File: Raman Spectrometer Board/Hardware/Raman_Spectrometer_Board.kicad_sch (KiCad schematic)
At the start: 16 parts, among them J1 RJ45_LED_Shielded, J2 Conn_01x05_Pin, J3 Conn_01x03_Pin, Q1 BSS138, U1 Teensy4.1_DEV-16771, U2 OKI

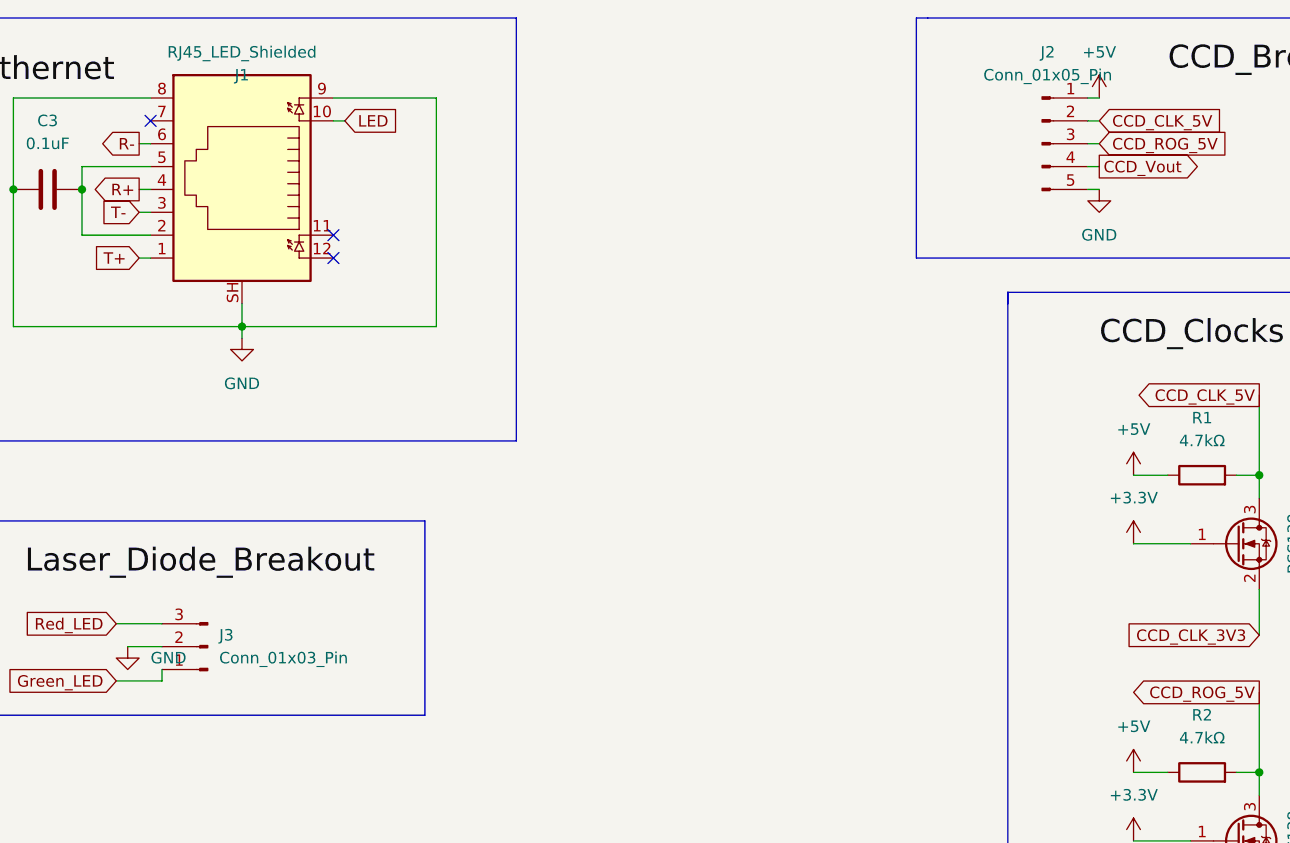
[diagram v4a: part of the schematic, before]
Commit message: fix: switched connectors to Molex
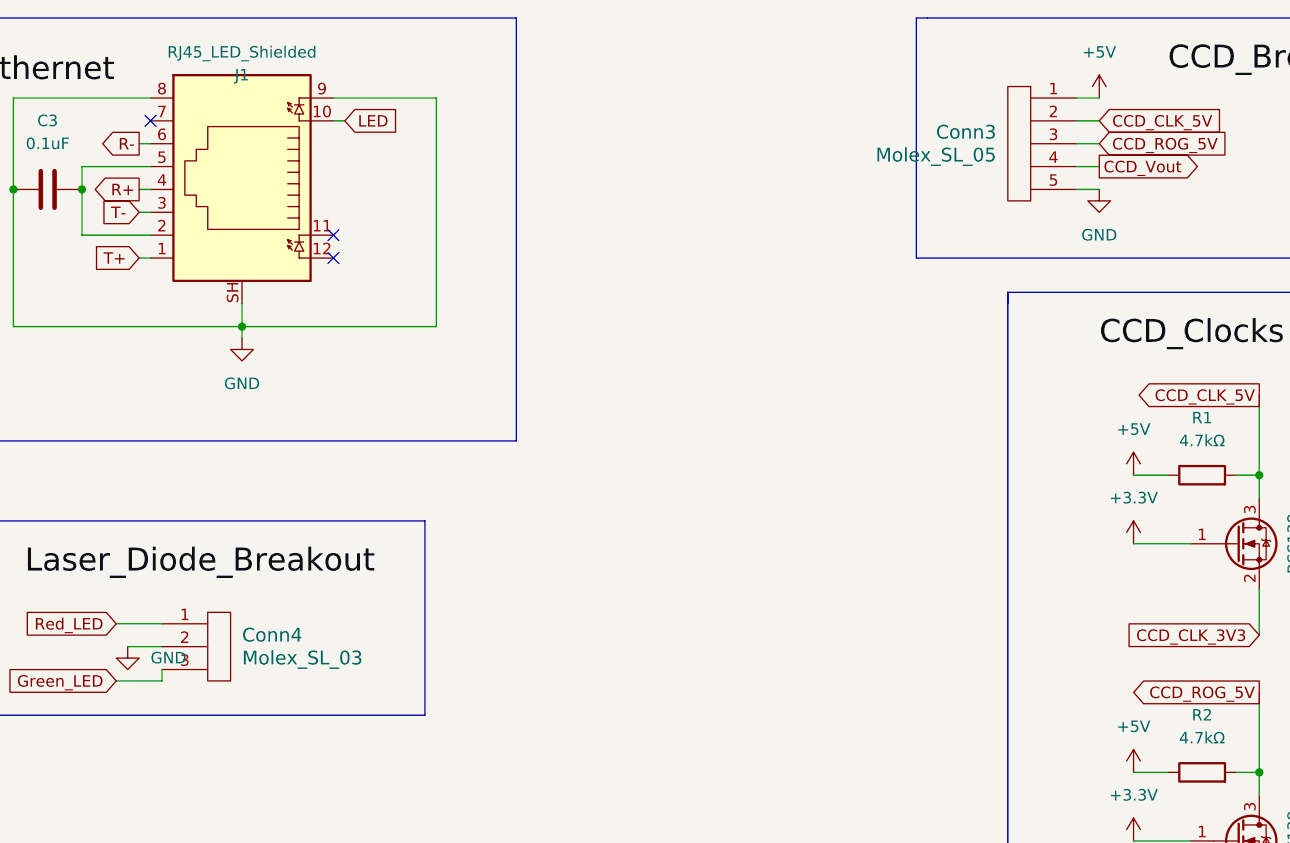
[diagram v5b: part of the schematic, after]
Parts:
- removed J2: Conn_01x05_Pin, symbol Connector:Conn_01x05_Pin
- removed J3: Conn_01x03_Pin, symbol Connector:Conn_01x03_Pin
- added Conn3: Molex_SL_05, symbol MRDT_Connectors:Molex_SL_05
- added Conn4: Molex_SL_03, symbol MRDT_Connectors:Molex_SL_03
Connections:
- net +5V: now also Conn3.1
- net CCD_CLK_5V: now also Conn3.2
- net CCD_ROG_5V: now also Conn3.3
- net CCD_Vout: now also Conn3.4
- net GND: now also Conn3.5, Conn4.2
- net Green_LED: now also Conn4.3
- net Red_LED: now also Conn4.1
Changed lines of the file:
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@@
-    (stroke (width 0) (type default))
-  )
-  (wire (pts (xy 243.84 22.86) (xy 245.11 22.86))
     (stroke (width 0) (type default))
   )
@@
     (stroke (width 0) (type default))
   )
+  (wire (pts (xy 242.57 22.86) (xy 245.11 22.86))
+    (stroke (width 0) (type default))
+  )
   (wire (pts (xy 82.55 135.89) (xy 81.28 135.89))
     (stroke (width 0) (type default))
@@
     (stroke (width 0) (type default))
   )
-  (wire (pts (xy 243.84 33.02) (xy 245.11 33.02))
+  (wire (pts (xy 242.57 33.02) (xy 245.11 33.02))
     (stroke (width 0) (type default))
   )
@@
     (stroke (width 0) (type default))
   )
-  (wire (pts (xy 243.84 27.94) (xy 245.11 27.94))
+  (wire (pts (xy 242.57 27.94) (xy 245.11 27.94))
     (stroke (width 0) (type default))
   )
@@
     (stroke (width 0) (type default))
   )
-  (wire (pts (xy 243.84 25.4) (xy 245.11 25.4))
-    (stroke (width 0) (type default))
-  )
   (polyline (pts (xy 115.57 13.97) (xy 115.57 60.96))
     (stroke (width 0) (type default))
@@
     (stroke (width 0) (type default))
   )
-  (wire (pts (xy 243.84 30.48) (xy 245.11 30.48))
+  (wire (pts (xy 242.57 30.48) (xy 245.11 30.48))
     (stroke (width 0) (type default))
   )
@@
   )
   (polyline (pts (xy 234.95 121.92) (xy 242.57 121.92))
+    (stroke (width 0) (type default))
+  )
+  (wire (pts (xy 242.57 25.4) (xy 245.11 25.4))
     (stroke (width 0) (type default))
   )
@@
     )
   )
+  (symbol (lib_id "MRDT_Connectors:Molex_SL_03") (at 146.05 87.63 0) (unit 1)
+    (in_bom yes) (on_board yes) (dnp no) (fields_autoplaced)
+    (property "Reference" "Conn4" (at 149.86 82.55 0)
+      (effects (font (size 1.524 1.524)) (justify left))
+    )
+    (property "Value" "Molex_SL_03" (at 149.86 85.09 0)
+      (effects (font (size 1.524 1.524)) (justify left))
+    )
+    (property "Footprint" "" (at 146.05 87.63 0)
+      (effects (font (size 1.524 1.524)) hide)
+    )
+    (property "Datasheet" "" (at 146.05 87.63 0)
+      (effects (font (size 1.524 1.524)) hide)
+    )
+    (pin "1")
+    (pin "2")
+    (pin "3")
+    (instances
+      (project "Raman_Spectrometer_Board"
+        (path "/dd57774e-6364-4f58-a24d-9970470de2f9"
+          (reference "Conn4") (unit 1)
+        )
+      )
+    )
+  )
   (symbol (lib_id "Device:C") (at 128.27 33.02 270) (unit 1)
     (in_bom yes) (on_board yes) (dnp no) (fields_autoplaced)
@@
         (path "/dd57774e-6364-4f58-a24d-9970470de2f9"
           (reference "#PWR01") (unit 1)
-        )
-      )
-    )
-  )
-  (symbol (lib_id "Connector:Conn_01x05_Pin") (at 238.76 27.94 0) (unit 1)
-    (in_bom yes) (on_board yes) (dnp no) (fields_autoplaced)
-    (property "Reference" "J2" (at 239.395 17.78 0)
-      (effects (font (size 1.27 1.27)))
-    )
-    (property "Value" "Conn_01x05_Pin" (at 239.395 20.32 0)
-      (effects (font (size 1.27 1.27)))
-    )
-    (property "Footprint" "" (at 238.76 27.94 0)
-      (effects (font (size 1.27 1.27)) hide)
-    )
-    (property "Datasheet" "~" (at 238.76 27.94 0)
-      (effects (font (size 1.27 1.27)) hide)
-    )
-    (pin "1")
-    (pin "2")
-    (pin "3")
-    (pin "4")
-    (pin "5")
-    (instances
-      (project "Raman_Spectrometer_Board"
-        (path "/dd57774e-6364-4f58-a24d-9970470de2f9"
-          (reference "J2") (unit 1)
-        )
-      )
-    )
-  )
-  (symbol (lib_id "Connector:Conn_01x03_Pin") (at 146.05 83.82 180) (unit 1)
-    (in_bom yes) (on_board yes) (dnp no) (fields_autoplaced)
-    (property "Reference" "J3" (at 147.32 82.55 0)
-      (effects (font (size 1.27 1.27)) (justify right))
-    )
-    (property "Value" "Conn_01x03_Pin" (at 147.32 85.09 0)
-      (effects (font (size 1.27 1.27)) (justify right))
-    )
-    (property "Footprint" "" (at 146.05 83.82 0)
-      (effects (font (size 1.27 1.27)) hide)
-    )
-    (property "Datasheet" "~" (at 146.05 83.82 0)
-      (effects (font (size 1.27 1.27)) hide)
-    )
-    (pin "1")
-    (pin "2")
-    (pin "3")
-    (instances
-      (project "Raman_Spectrometer_Board"
-        (path "/dd57774e-6364-4f58-a24d-9970470de2f9"
-          (reference "J3") (unit 1)
         )
       )
@@
         )
       )
+    )
+  )
+  (symbol (lib_id "MRDT_Connectors:Molex_SL_05") (at 237.49 34.29 0) (mirror y) (unit 1)
+    (in_bom yes) (on_board yes) (dnp no)
+    (property "Reference" "Conn3" (at 233.68 26.67 0)
+      (effects (font (size 1.524 1.524)) (justify left))
+    )
+    (property "Value" "Molex_SL_05" (at 233.68 29.21 0)
+      (effects (font (size 1.524 1.524)) (justify left))
+    )
+    (property "Footprint" "" (at 237.49 34.29 0)
+      (effects (font (size 1.524 1.524)) hide)
+    )
+    (property "Datasheet" "" (at 237.49 34.29 0)
+      (effects (font (size 1.524 1.524)) hide)
+    )
+    (pin "1")
+    (pin "2")
+    (pin "3")
+    (pin "4")
+    (pin "5")
+    (instances
+      (project "Raman_Spectrometer_Board"
+        (path "/dd57774e-6364-4f58-a24d-9970470de2f9"
+          (reference "Conn3") (unit 1)
+        )
+      )

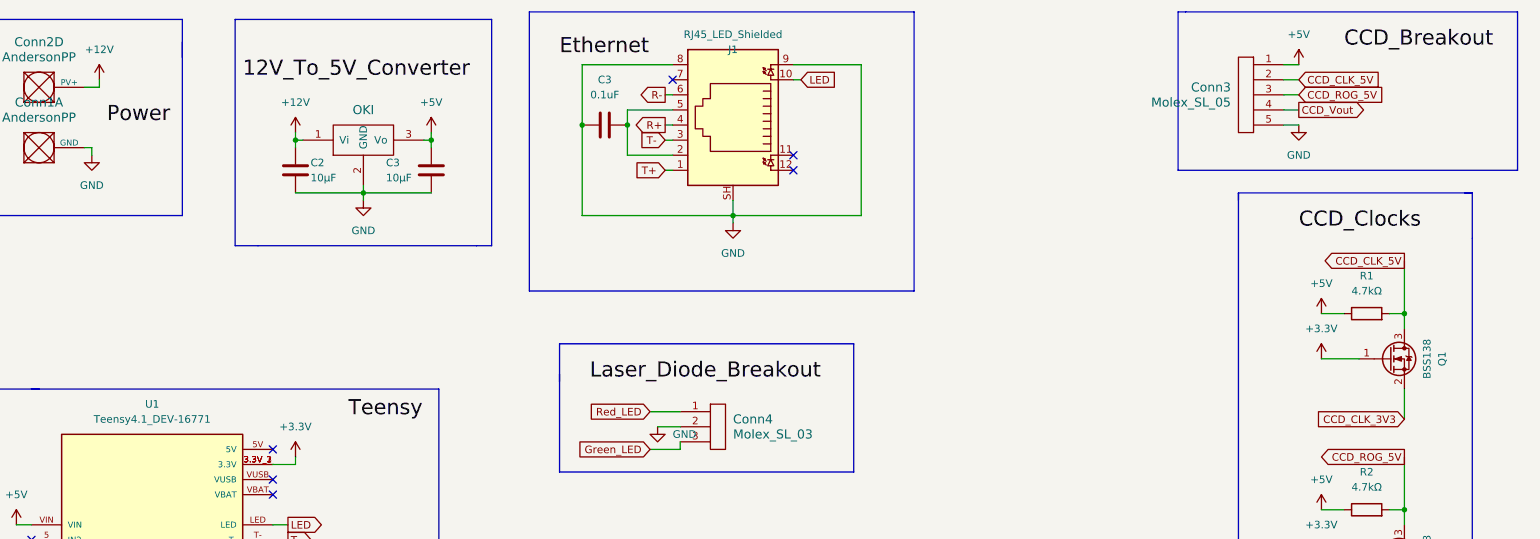
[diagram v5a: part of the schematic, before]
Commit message: fix: replaced net labels with text
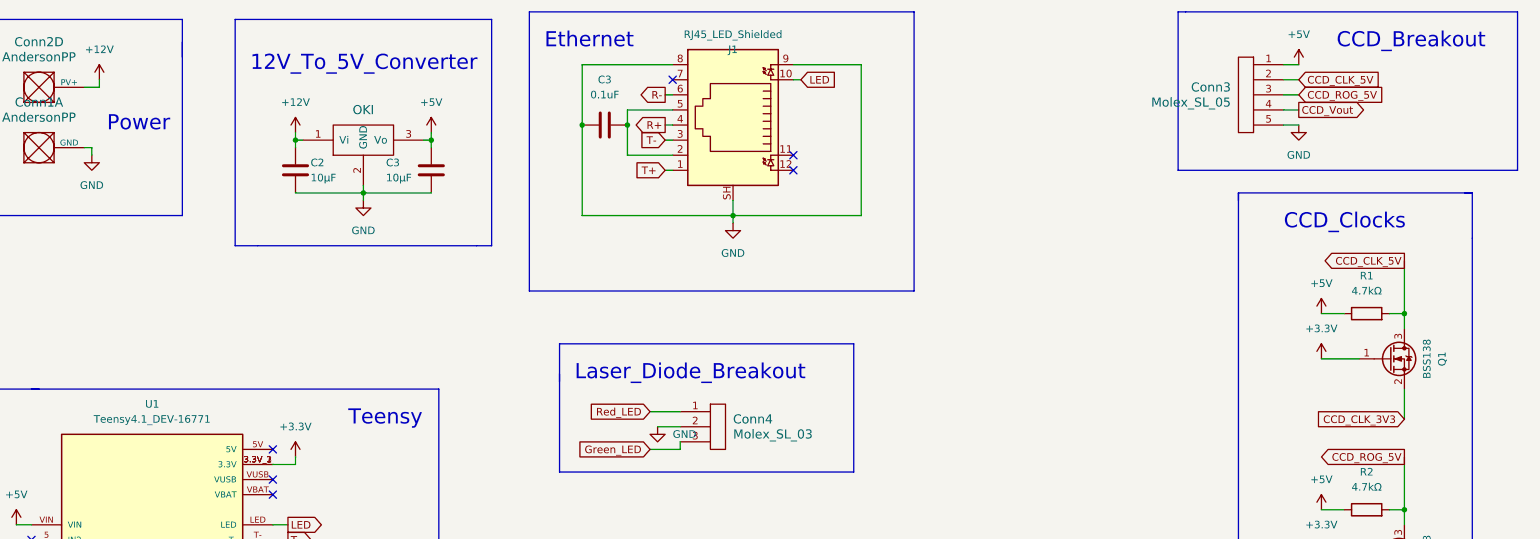
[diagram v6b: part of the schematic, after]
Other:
- note added: "12V_To_5V_Converter"
- note added: "CCD_Breakout"
- note added: "CCD_Clocks"
- note added: "Ethernet"
- note added: "Laser_Diode_Breakout"
- note added: "Power"
- note added: "Teensy"
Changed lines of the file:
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@@
     (stroke (width 0) (type default))
   )
-  (label "Laser_Diode_Breakout" (at 125.73 76.2 0) (fields_autoplaced)
+  (text "Ethernet" (at 118.11 20.32 0)
     (effects (font (size 2.54 2.54)) (justify left bottom))
   )
-  (label "CCD_Clocks" (at 245.11 50.8 0) (fields_autoplaced)
+  (text "Teensy" (at 85.09 83.82 0)
     (effects (font (size 2.54 2.54)) (justify left bottom))
   )
-  (label "Teensy" (at 85.09 82.55 0) (fields_autoplaced)
+  (text "CCD_Clocks" (at 242.57 50.8 0)
     (effects (font (size 2.54 2.54)) (justify left bottom))
   )
-  (label "CCD_Breakout" (at 252.73 20.32 0) (fields_autoplaced)
+  (text "12V_To_5V_Converter" (at 68.58 24.13 0)
     (effects (font (size 2.54 2.54)) (justify left bottom))
   )
-  (label "Ethernet" (at 120.65 21.59 0) (fields_autoplaced)
+  (text "CCD_Breakout" (at 251.46 20.32 0)
     (effects (font (size 2.54 2.54)) (justify left bottom))
   )
-  (label "Power" (at 44.45 33.02 0) (fields_autoplaced)
+  (text "Power" (at 44.45 34.29 0)
     (effects (font (size 2.54 2.54)) (justify left bottom))
   )
-  (label "12V_To_5V_Converter" (at 67.31 25.4 0) (fields_autoplaced)
+  (text "Laser_Diode_Breakout" (at 123.19 76.2 0)
     (effects (font (size 2.54 2.54)) (justify left bottom))
   )

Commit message: misc schematic review changes
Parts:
- removed Conn2: AndersonPP, symbol MRDT_Connectors:AndersonPP
- removed R3: 17Ω, symbol Device:R
- removed R4: 24Ω, symbol Device:R
- added unit 3 of Conn1
- C3: value 0.1uF -> 0.1µF
- R1, R2: value 4.7kΩ -> 4.7k
- renumbered Conn3 to Conn2, Conn4 to Conn3
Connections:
- net +12V: now also Conn1.3 (V+Act)
- net Green_LED: now also U1.37 (CS3)
- net Red_LED: now also U1.36 (CS2)
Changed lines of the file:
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@@
-    (stroke (width 0) (type default))
-  )
-  (wire (pts (xy 82.55 135.89) (xy 81.28 135.89))
     (stroke (width 0) (type default))
   )
@@
   )
   (wire (pts (xy 40.64 26.67) (xy 43.18 26.67))
-    (stroke (width 0) (type default))
-  )
-  (wire (pts (xy 82.55 138.43) (xy 81.28 138.43))
     (stroke (width 0) (type default))
   )
@@
     )
   )
-  (global_label "Green_LED" (shape output) (at 82.55 135.89 0) (fields_autoplaced)
+  (global_label "Green_LED" (shape output) (at 73.66 135.89 0) (fields_autoplaced)
     (effects (font (size 1.27 1.27)) (justify left))
-    (property "Intersheetrefs" "${INTERSHEET_REFS}" (at 95.3323 135.89 0)
+    (property "Intersheetrefs" "${INTERSHEET_REFS}" (at 86.4423 135.89 0)
       (effects (font (size 1.27 1.27)) (justify left) hide)
     )
@@
     )
   )
-  (global_label "Red_LED" (shape output) (at 82.55 138.43 0) (fields_autoplaced)
+  (global_label "Red_LED" (shape output) (at 73.66 138.43 0) (fields_autoplaced)
     (effects (font (size 1.27 1.27)) (justify left))
-    (property "Intersheetrefs" "${INTERSHEET_REFS}" (at 93.4575 138.43 0)
+    (property "Intersheetrefs" "${INTERSHEET_REFS}" (at 84.5675 138.43 0)
       (effects (font (size 1.27 1.27)) (justify left) hide)
     )
@@
   (symbol (lib_id "MRDT_Connectors:Molex_SL_03") (at 146.05 87.63 0) (unit 1)
     (in_bom yes) (on_board yes) (dnp no) (fields_autoplaced)
-    (property "Reference" "Conn4" (at 149.86 82.55 0)
+    (property "Reference" "Conn3" (at 149.86 82.55 0)
       (effects (font (size 1.524 1.524)) (justify left))
     )
@@
       (project "Raman_Spectrometer_Board"
         (path "/dd57774e-6364-4f58-a24d-9970470de2f9"
-          (reference "Conn4") (unit 1)
+          (reference "Conn3") (unit 1)
         )
       )
@@
       (effects (font (size 1.27 1.27)))
     )
-    (property "Value" "0.1uF" (at 128.27 27.94 90)
+    (property "Value" "0.1µF" (at 128.27 27.94 90)
       (effects (font (size 1.27 1.27)))
     )
@@
     )
   )
-  (symbol (lib_id "Device:R") (at 77.47 135.89 90) (unit 1)
-    (in_bom yes) (on_board yes) (dnp no) (fields_autoplaced)
-    (property "Reference" "R3" (at 77.47 129.54 90)
-      (effects (font (size 1.27 1.27)))
-    )
-    (property "Value" "17Ω" (at 77.47 132.08 90)
-      (effects (font (size 1.27 1.27)))
-    )
-    (property "Footprint" "" (at 77.47 137.668 90)
-      (effects (font (size 1.27 1.27)) hide)
-    )
-    (property "Datasheet" "~" (at 77.47 135.89 0)
-      (effects (font (size 1.27 1.27)) hide)
-    )
-    (pin "1")
-    (pin "2")
-    (instances
-      (project "Raman_Spectrometer_Board"
-        (path "/dd57774e-6364-4f58-a24d-9970470de2f9"
-          (reference "R3") (unit 1)
-        )
-      )
-    )
-  )
   (symbol (lib_id "power:GND") (at 149.86 49.53 0) (unit 1)
     (in_bom yes) (on_board yes) (dnp no) (fields_autoplaced)
@@
   )
   (symbol (lib_id "MRDT_Connectors:AndersonPP") (at 30.48 39.37 0) (unit 1)
-    (in_bom yes) (on_board yes) (dnp no) (fields_autoplaced)
+    (in_bom yes) (on_board yes) (dnp no)
     (property "Reference" "Conn1" (at 33.02 29.21 0)
       (effects (font (size 1.524 1.524)))
@@
     )
   )
-  (symbol (lib_id "Device:R") (at 77.47 138.43 90) (unit 1)
-    (in_bom yes) (on_board yes) (dnp no)
-    (property "Reference" "R4" (at 77.47 140.97 90)
-      (effects (font (size 1.27 1.27)))
-    )
-    (property "Value" "24Ω" (at 77.47 143.51 90)
-      (effects (font (size 1.27 1.27)))
-    )
-    (property "Footprint" "" (at 77.47 140.208 90)
-      (effects (font (size 1.27 1.27)) hide)
-    )
-    (property "Datasheet" "~" (at 77.47 138.43 0)
-      (effects (font (size 1.27 1.27)) hide)
-    )
-    (pin "1")
-    (pin "2")
-    (instances
-      (project "Raman_Spectrometer_Board"
-        (path "/dd57774e-6364-4f58-a24d-9970470de2f9"
-          (reference "R4") (unit 1)
-        )
-      )
-    )
-  )
   (symbol (lib_id "power:+3.3V") (at 248.92 105.41 0) (unit 1)
     (in_bom yes) (on_board yes) (dnp no) (fields_autoplaced)
@@
     )
   )
-  (symbol (lib_id "MRDT_Connectors:AndersonPP") (at 30.48 29.21 0) (unit 4)
-    (in_bom yes) (on_board yes) (dnp no) (fields_autoplaced)
-    (property "Reference" "Conn2" (at 33.02 19.05 0)
+  (symbol (lib_id "MRDT_Connectors:AndersonPP") (at 30.48 29.21 0) (unit 3)
+    (in_bom yes) (on_board yes) (dnp no) (fields_autoplaced)
+    (property "Reference" "Conn1" (at 33.02 19.05 0)
       (effects (font (size 1.524 1.524)))
     )
@@
       (project "Raman_Spectrometer_Board"
         (path "/dd57774e-6364-4f58-a24d-9970470de2f9"
-          (reference "Conn2") (unit 4)
+          (reference "Conn1") (unit 3)
         )
       )
@@
   )
   (symbol (lib_id "Device:R") (at 256.54 64.77 90) (unit 1)
-    (in_bom yes) (on_board yes) (dnp no) (fields_autoplaced)
-    (property "Reference" "R1" (at 256.54 58.42 90)
-      (effects (font (size 1.27 1.27)))
-    )
-    (property "Value" "4.7kΩ" (at 256.54 60.96 90)
+    (in_bom yes) (on_board yes) (dnp no)
+    (property "Reference" "R1" (at 256.54 62.23 90)
+      (effects (font (size 1.27 1.27)))
+    )
+    (property "Value" "4.7k" (at 256.54 64.77 90)
       (effects (font (size 1.27 1.27)))
     )
@@
   )
   (symbol (lib_id "Device:R") (at 256.54 97.79 90) (unit 1)
-    (in_bom yes) (on_board yes) (dnp no) (fields_autoplaced)
-    (property "Reference" "R2" (at 256.54 91.44 90)
-      (effects (font (size 1.27 1.27)))
-    )
-    (property "Value" "4.7kΩ" (at 256.54 93.98 90)
+    (in_bom yes) (on_board yes) (dnp no)
+    (property "Reference" "R2" (at 256.54 95.25 90)
+      (effects (font (size 1.27 1.27)))
+    )
+    (property "Value" "4.7k" (at 256.54 97.79 90)
       (effects (font (size 1.27 1.27)))
     )
@@
   (symbol (lib_id "MRDT_Connectors:Molex_SL_05") (at 237.49 34.29 0) (mirror y) (unit 1)
     (in_bom yes) (on_board yes) (dnp no)
-    (property "Reference" "Conn3" (at 233.68 26.67 0)
+    (property "Reference" "Conn2" (at 233.68 26.67 0)
       (effects (font (size 1.524 1.524)) (justify left))
     )
@@
       (project "Raman_Spectrometer_Board"
         (path "/dd57774e-6364-4f58-a24d-9970470de2f9"
-          (reference "Conn3") (unit 1)
-        )
-      )
+          (reference "Conn2") (unit 1)
+        )
+      )

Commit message: fix: use mosfets to control diodes
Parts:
- removed Conn3: Molex_SL_03, symbol MRDT_Connectors:Molex_SL_03
- added Conn3: Molex_SL_04, symbol MRDT_Connectors:Molex_SL_04
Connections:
- net +5V: now also Conn3.1
- net GND: now also Conn3.4
- net Green_LED: now also Conn3.3
- net Red_LED: now also Conn3.2
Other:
- moved on the sheet: Conn2
